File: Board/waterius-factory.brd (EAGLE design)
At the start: 13.5 x 60 mm, 23 parts, among them IC1 TINY13-20SU, U2 MCP1700T-3302E/TT, U3 ESP01

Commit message: readme
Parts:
- added PAD1: MOUNT-HOLE2.8, holes:2,8
- JP1: value (none) -> + -
- moved R7 1.97 mm to (8.93, 23.2), turned to 0 degrees
- moved C3 1.85 mm to (8.93, 26.1)
- moved R5 1.51 mm to (3.31, 23.3)
- moved U3 1.48 mm to (7.28, 25.8)
- moved R6 1.43 mm to (3.27, 26.1), turned to 180 degrees
- moved IC1 1.35 mm to (4.00, 33.4)
- moved R10 1.35 mm to (9.53, 29.4)
- moved R2 1.35 mm to (9.59, 33.4)
- moved C4 1.35 mm to (9.54, 37.0)
- moved JP1 1.10 mm to (10.5, 4.43)
- moved C2 0.98 mm to (2.60, 11.0)
- moved LED1 0.98 mm to (11.0, 9.98)
- moved LOG 0.98 mm to (11.0, 14.0)
- moved R8 0.98 mm to (7.30, 11.0)
- moved C1 0.98 mm to (7.00, 6.72)
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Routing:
- net WAKE_UP: track 18.6 -> 29.1 mm
- net SDA: track 18.2 -> 12.0 mm, vias 1 -> 0
- net SCK: track 29.5 -> 25.9 mm, vias 2 -> 0
- net +3V3: track 34.3 -> 37.5 mm, vias 0 -> 2
- net GND: track 57.8 -> 56.2 mm
- net N$3: track 4.07 -> 5.06 mm
- net IN1: track 14.8 -> 13.9 mm
- net IN2: track 10.6 -> 9.94 mm
- net GND1: track 37.8 -> 37.3 mm
- added copper zone on layer 16, net N$11
- added copper zone on layer 1, net N$9

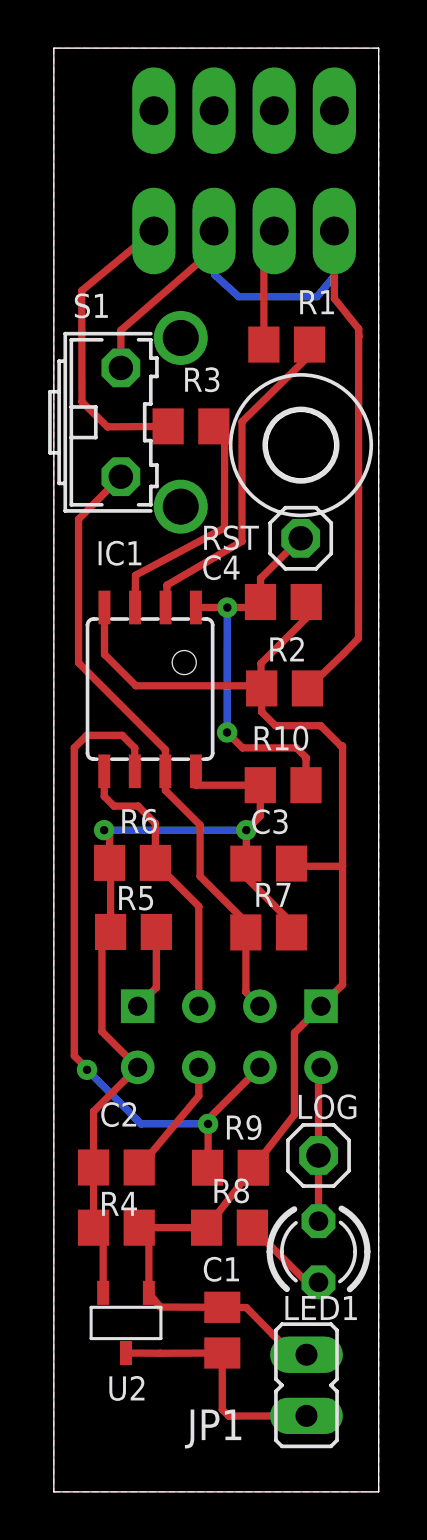
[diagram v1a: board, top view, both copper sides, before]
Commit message: 1. Добавлен U3 наверх и низ платы
2. подписан каждый пин ESP
3. Позиционные обозначения многие переставлены
4. В схеме изменён компонент на MCP1700-3002
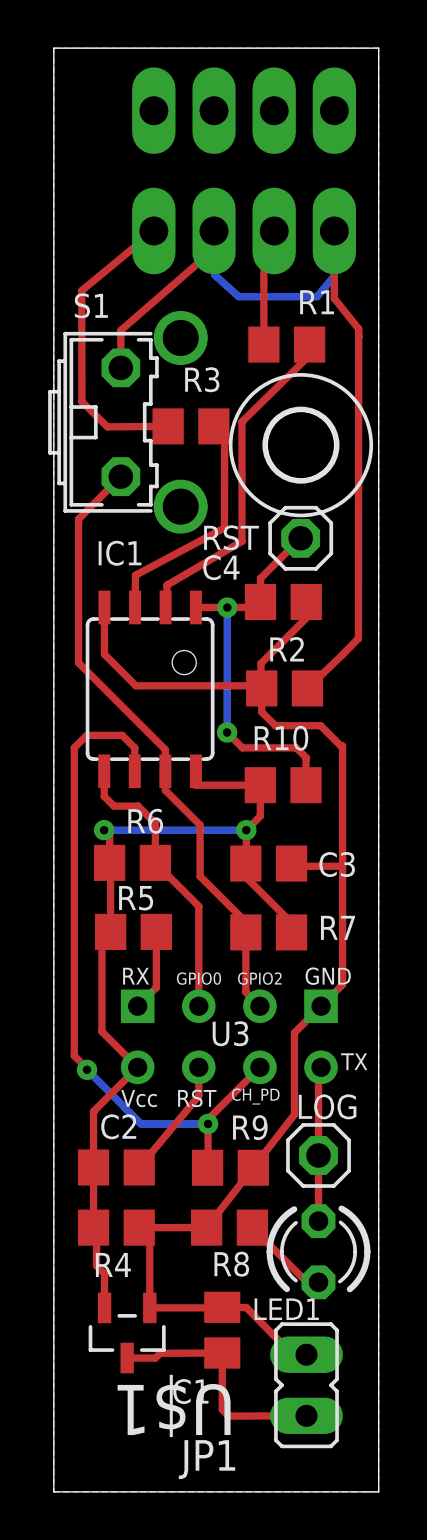
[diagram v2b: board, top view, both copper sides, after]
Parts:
- removed U2: MCP1700T-3302E/TT, MCP1700T-3302E_TT:MCP1700T-3302E/TT
- added U$1: MCP1700T-3002E/TT, Microchip_By_element14_Batch_1:SOT95P237X112-3N
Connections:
- removed net +3V3: C2.1, C3.1, IC1.8, R10.2, R4.2, R5.2, R6.2, R7.2, U2.VOUT, U3.VCC
- new net +3V: C2.1, C3.1, IC1.8, R10.2, R4.2, R5.2, R6.2, R7.2, U$1.2, U3.VCC
- net GND: now also U$1.1; no longer U2.GND
- net N$1: now also U$1.3; no longer U2.VIN
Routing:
- net +3V: track 0.00 -> 38.8 mm, vias 0 -> 2
- net +3V3: track 37.5 -> 0.00 mm, vias 2 -> 0
- net GND: track 56.2 -> 57.1 mm
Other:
- board text added: "CH_PD"
- board text added: "GND"
- board text added: "GPIO0"
- board text added: "GPIO2"
- board text added: "RST"
- board text added: "RX"
- board text added: "TX"
- board text added: "U3"
- board text added: "Vcc"
